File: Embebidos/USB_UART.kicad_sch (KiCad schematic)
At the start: 9 parts

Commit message: Corrección de anotaciones
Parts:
- renumbered C2 to C5, C3 to C6, C1 to C7, Q2 to Q1, Q1 to Q2, R1 to R12, R2 to R13
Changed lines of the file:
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@@
   (symbol (lib_id "power:VBUS") (at 102.87 86.36 0) (unit 1)
     (in_bom yes) (on_board yes) (fields_autoplaced)
-    (property "Reference" "#PWR?" (id 0) (at 102.87 90.17 0)
+    (property "Reference" "#PWR013" (id 0) (at 102.87 90.17 0)
       (effects (font (size 1.27 1.27)) hide)
     )
@@
   (symbol (lib_id "power:GND") (at 130.81 130.81 0) (unit 1)
     (in_bom yes) (on_board yes) (fields_autoplaced)
-    (property "Reference" "#PWR?" (id 0) (at 130.81 137.16 0)
+    (property "Reference" "#PWR016" (id 0) (at 130.81 137.16 0)
       (effects (font (size 1.27 1.27)) hide)
     )
@@
   (symbol (lib_id "Device:R") (at 184.15 90.17 90) (unit 1)
     (in_bom yes) (on_board yes) (fields_autoplaced)
-    (property "Reference" "R1" (id 0) (at 184.15 83.82 90))
+    (property "Reference" "R12" (id 0) (at 184.15 83.82 90))
     (property "Value" "~" (id 1) (at 184.15 86.36 90))
     (property "Footprint" "" (id 2) (at 184.15 91.948 90)
@@
   (symbol (lib_id "power:GND") (at 111.76 130.81 0) (unit 1)
     (in_bom yes) (on_board yes) (fields_autoplaced)
-    (property "Reference" "#PWR?" (id 0) (at 111.76 137.16 0)
+    (property "Reference" "#PWR014" (id 0) (at 111.76 137.16 0)
       (effects (font (size 1.27 1.27)) hide)
     )
@@
   (symbol (lib_id "power:GND") (at 92.71 129.54 0) (unit 1)
     (in_bom yes) (on_board yes) (fields_autoplaced)
-    (property "Reference" "#PWR?" (id 0) (at 92.71 135.89 0)
+    (property "Reference" "#PWR012" (id 0) (at 92.71 135.89 0)
       (effects (font (size 1.27 1.27)) hide)
     )
@@
   (symbol (lib_id "power:+3.3V") (at 92.71 116.84 0) (unit 1)
     (in_bom yes) (on_board yes) (fields_autoplaced)
-    (property "Reference" "#PWR?" (id 0) (at 92.71 120.65 0)
+    (property "Reference" "#PWR011" (id 0) (at 92.71 120.65 0)
       (effects (font (size 1.27 1.27)) hide)
     )
@@
   (symbol (lib_id "Device:C") (at 97.79 123.19 0) (unit 1)
     (in_bom yes) (on_board yes) (fields_autoplaced)
-    (property "Reference" "C3" (id 0) (at 101.6 121.9199 0)
+    (property "Reference" "C6" (id 0) (at 101.6 121.9199 0)
       (effects (font (size 1.27 1.27)) (justify left))
     )
@@
   (symbol (lib_id "Transistor_BJT:BC847") (at 196.85 114.3 0) (mirror x) (unit 1)
     (in_bom yes) (on_board yes) (fields_autoplaced)
-    (property "Reference" "Q1" (id 0) (at 201.93 113.0299 0)
+    (property "Reference" "Q2" (id 0) (at 201.93 113.0299 0)
       (effects (font (size 1.27 1.27)) (justify left))
     )
@@
   (symbol (lib_id "power:GND") (at 81.28 104.14 0) (unit 1)
     (in_bom yes) (on_board yes) (fields_autoplaced)
-    (property "Reference" "#PWR?" (id 0) (at 81.28 110.49 0)
+    (property "Reference" "#PWR010" (id 0) (at 81.28 110.49 0)
       (effects (font (size 1.27 1.27)) hide)
     )
@@
   (symbol (lib_id "power:+3.3V") (at 130.81 66.04 0) (unit 1)
     (in_bom yes) (on_board yes) (fields_autoplaced)
-    (property "Reference" "#PWR?" (id 0) (at 130.81 69.85 0)
+    (property "Reference" "#PWR015" (id 0) (at 130.81 69.85 0)
       (effects (font (size 1.27 1.27)) hide)
     )
@@
   (symbol (lib_id "Device:C") (at 86.36 123.19 0) (unit 1)
     (in_bom yes) (on_board yes) (fields_autoplaced)
-    (property "Reference" "C2" (id 0) (at 90.17 121.9199 0)
+    (property "Reference" "C5" (id 0) (at 90.17 121.9199 0)
       (effects (font (size 1.27 1.27)) (justify left))
     )
@@
   (symbol (lib_id "Device:R") (at 184.15 114.3 90) (unit 1)
     (in_bom yes) (on_board yes) (fields_autoplaced)
-    (property "Reference" "R2" (id 0) (at 184.15 107.95 90))
+    (property "Reference" "R13" (id 0) (at 184.15 107.95 90))
     (property "Value" "~" (id 1) (at 184.15 110.49 90))
     (property "Footprint" "" (id 2) (at 184.15 116.078 90)
@@
   (symbol (lib_id "Device:C") (at 111.76 124.46 0) (unit 1)
     (in_bom yes) (on_board yes) (fields_autoplaced)
-    (property "Reference" "C1" (id 0) (at 115.57 123.1899 0)
+    (property "Reference" "C7" (id 0) (at 115.57 123.1899 0)
       (effects (font (size 1.27 1.27)) (justify left))
     )
@@
   (symbol (lib_id "Transistor_BJT:BC847") (at 196.85 90.17 0) (unit 1)
     (in_bom yes) (on_board yes) (fields_autoplaced)
-    (property "Reference" "Q2" (id 0) (at 201.93 88.8999 0)
-      (effects (font (size 1.27 1.27)) (justify left))
-    )
+    (property "Reference" "Q1" (id 0) (at 201.93 88.8999 0)
+      (effects (font (size 1.27 1.27)) (justify left))
+    )

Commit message: anotaciones_fix
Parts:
- renumbered R12 to R13, R13 to R14
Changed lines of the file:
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@@
   (symbol (lib_id "power:VBUS") (at 102.87 86.36 0) (unit 1)
     (in_bom yes) (on_board yes) (fields_autoplaced)
-    (property "Reference" "#PWR013" (id 0) (at 102.87 90.17 0)
+    (property "Reference" "#PWR014" (id 0) (at 102.87 90.17 0)
       (effects (font (size 1.27 1.27)) hide)
     )
@@
   (symbol (lib_id "power:GND") (at 130.81 130.81 0) (unit 1)
     (in_bom yes) (on_board yes) (fields_autoplaced)
-    (property "Reference" "#PWR016" (id 0) (at 130.81 137.16 0)
+    (property "Reference" "#PWR017" (id 0) (at 130.81 137.16 0)
       (effects (font (size 1.27 1.27)) hide)
     )
@@
   (symbol (lib_id "Device:R") (at 184.15 90.17 90) (unit 1)
     (in_bom yes) (on_board yes) (fields_autoplaced)
-    (property "Reference" "R12" (id 0) (at 184.15 83.82 90))
+    (property "Reference" "R13" (id 0) (at 184.15 83.82 90))
     (property "Value" "~" (id 1) (at 184.15 86.36 90))
     (property "Footprint" "" (id 2) (at 184.15 91.948 90)
@@
   (symbol (lib_id "power:GND") (at 111.76 130.81 0) (unit 1)
     (in_bom yes) (on_board yes) (fields_autoplaced)
-    (property "Reference" "#PWR014" (id 0) (at 111.76 137.16 0)
+    (property "Reference" "#PWR015" (id 0) (at 111.76 137.16 0)
       (effects (font (size 1.27 1.27)) hide)
     )
@@
   (symbol (lib_id "power:GND") (at 92.71 129.54 0) (unit 1)
     (in_bom yes) (on_board yes) (fields_autoplaced)
-    (property "Reference" "#PWR012" (id 0) (at 92.71 135.89 0)
+    (property "Reference" "#PWR013" (id 0) (at 92.71 135.89 0)
       (effects (font (size 1.27 1.27)) hide)
     )
@@
   (symbol (lib_id "power:+3.3V") (at 92.71 116.84 0) (unit 1)
     (in_bom yes) (on_board yes) (fields_autoplaced)
-    (property "Reference" "#PWR011" (id 0) (at 92.71 120.65 0)
+    (property "Reference" "#PWR012" (id 0) (at 92.71 120.65 0)
       (effects (font (size 1.27 1.27)) hide)
     )
@@
   (symbol (lib_id "power:GND") (at 81.28 104.14 0) (unit 1)
     (in_bom yes) (on_board yes) (fields_autoplaced)
-    (property "Reference" "#PWR010" (id 0) (at 81.28 110.49 0)
+    (property "Reference" "#PWR011" (id 0) (at 81.28 110.49 0)
       (effects (font (size 1.27 1.27)) hide)
     )
@@
   (symbol (lib_id "power:+3.3V") (at 130.81 66.04 0) (unit 1)
     (in_bom yes) (on_board yes) (fields_autoplaced)
-    (property "Reference" "#PWR015" (id 0) (at 130.81 69.85 0)
+    (property "Reference" "#PWR016" (id 0) (at 130.81 69.85 0)
       (effects (font (size 1.27 1.27)) hide)
     )
@@
   (symbol (lib_id "Device:R") (at 184.15 114.3 90) (unit 1)
     (in_bom yes) (on_board yes) (fields_autoplaced)
-    (property "Reference" "R13" (id 0) (at 184.15 107.95 90))
+    (property "Reference" "R14" (id 0) (at 184.15 107.95 90))
     (property "Value" "~" (id 1) (at 184.15 110.49 90))
     (property "Footprint" "" (id 2) (at 184.15 116.078 90)

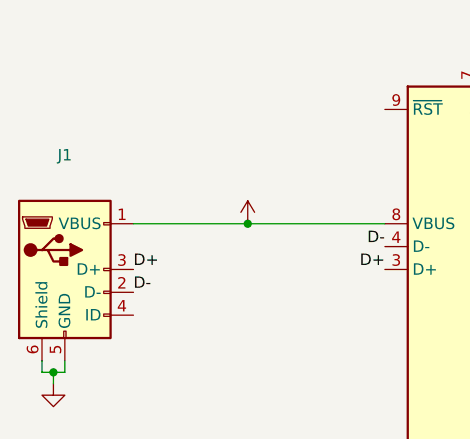
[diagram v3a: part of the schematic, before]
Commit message: Cambio de anotacion y Vcc ldr
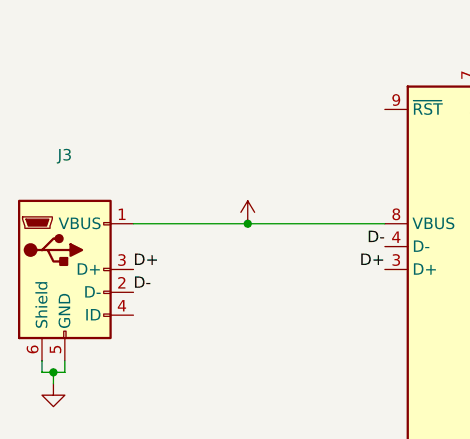
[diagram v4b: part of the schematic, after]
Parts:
- renumbered J1 to J3
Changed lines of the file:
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@@
   (symbol (lib_id "Connector:USB_B_Micro") (at 82.55 91.44 0) (unit 1)
     (in_bom yes) (on_board yes) (fields_autoplaced)
-    (property "Reference" "J1" (id 0) (at 82.55 78.74 0))
+    (property "Reference" "J3" (id 0) (at 82.55 78.74 0))
     (property "Value" "~" (id 1) (at 82.55 81.28 0))
     (property "Footprint" "" (id 2) (at 86.36 92.71 0)
@@
   (symbol (lib_id "power:VBUS") (at 102.87 86.36 0) (unit 1)
     (in_bom yes) (on_board yes) (fields_autoplaced)
-    (property "Reference" "#PWR014" (id 0) (at 102.87 90.17 0)
+    (property "Reference" "#PWR017" (id 0) (at 102.87 90.17 0)
       (effects (font (size 1.27 1.27)) hide)
     )
@@
   (symbol (lib_id "power:GND") (at 130.81 130.81 0) (unit 1)
     (in_bom yes) (on_board yes) (fields_autoplaced)
-    (property "Reference" "#PWR017" (id 0) (at 130.81 137.16 0)
+    (property "Reference" "#PWR020" (id 0) (at 130.81 137.16 0)
       (effects (font (size 1.27 1.27)) hide)
     )
@@
   (symbol (lib_id "power:GND") (at 111.76 130.81 0) (unit 1)
     (in_bom yes) (on_board yes) (fields_autoplaced)
-    (property "Reference" "#PWR015" (id 0) (at 111.76 137.16 0)
+    (property "Reference" "#PWR018" (id 0) (at 111.76 137.16 0)
       (effects (font (size 1.27 1.27)) hide)
     )
@@
   (symbol (lib_id "power:GND") (at 92.71 129.54 0) (unit 1)
     (in_bom yes) (on_board yes) (fields_autoplaced)
-    (property "Reference" "#PWR013" (id 0) (at 92.71 135.89 0)
+    (property "Reference" "#PWR016" (id 0) (at 92.71 135.89 0)
       (effects (font (size 1.27 1.27)) hide)
     )
@@
   (symbol (lib_id "power:+3.3V") (at 92.71 116.84 0) (unit 1)
     (in_bom yes) (on_board yes) (fields_autoplaced)
-    (property "Reference" "#PWR012" (id 0) (at 92.71 120.65 0)
+    (property "Reference" "#PWR015" (id 0) (at 92.71 120.65 0)
       (effects (font (size 1.27 1.27)) hide)
     )
@@
   (symbol (lib_id "power:GND") (at 81.28 104.14 0) (unit 1)
     (in_bom yes) (on_board yes) (fields_autoplaced)
-    (property "Reference" "#PWR011" (id 0) (at 81.28 110.49 0)
+    (property "Reference" "#PWR014" (id 0) (at 81.28 110.49 0)
       (effects (font (size 1.27 1.27)) hide)
     )
@@
   (symbol (lib_id "power:+3.3V") (at 130.81 66.04 0) (unit 1)
     (in_bom yes) (on_board yes) (fields_autoplaced)
-    (property "Reference" "#PWR016" (id 0) (at 130.81 69.85 0)
+    (property "Reference" "#PWR019" (id 0) (at 130.81 69.85 0)
       (effects (font (size 1.27 1.27)) hide)
     )

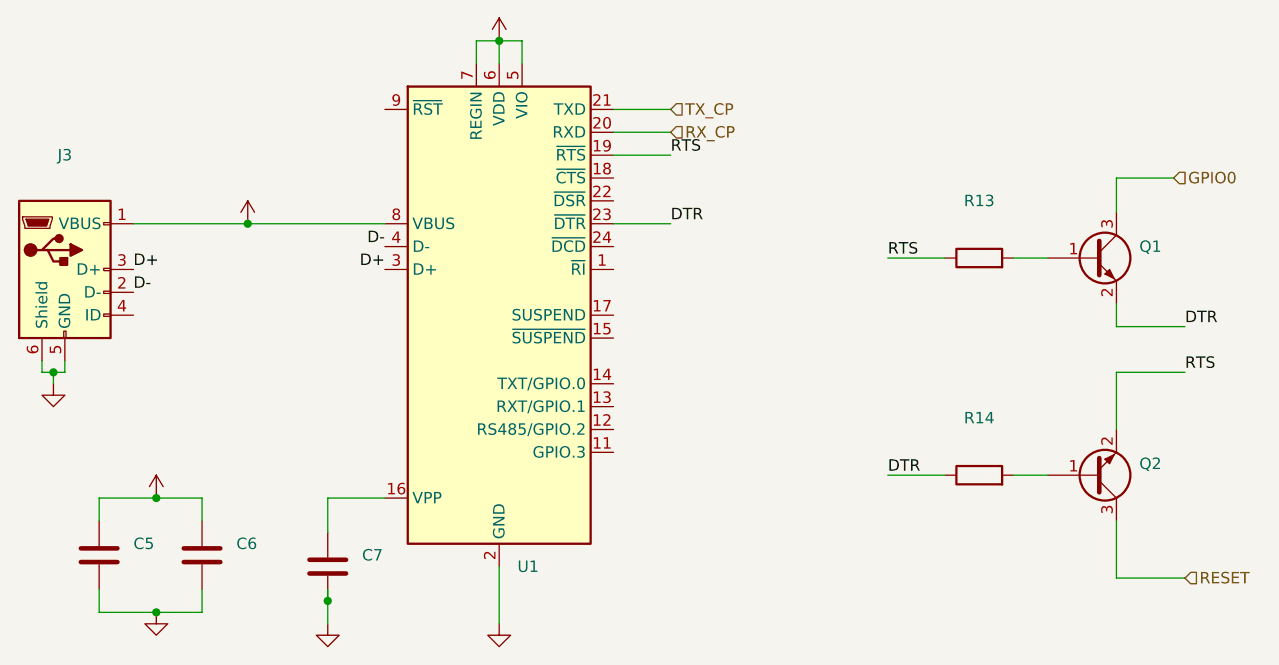
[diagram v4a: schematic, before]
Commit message: Cambios varios
-Conectores movidos a nueva hoja jerarquica

-Transistores DMP colocados en lices delanteras

-Jumpers ubicados para el uso del pin IO13 para SIM800 y LEDHW

-Etiqueta de "no conectado" ubicada en USB_UART
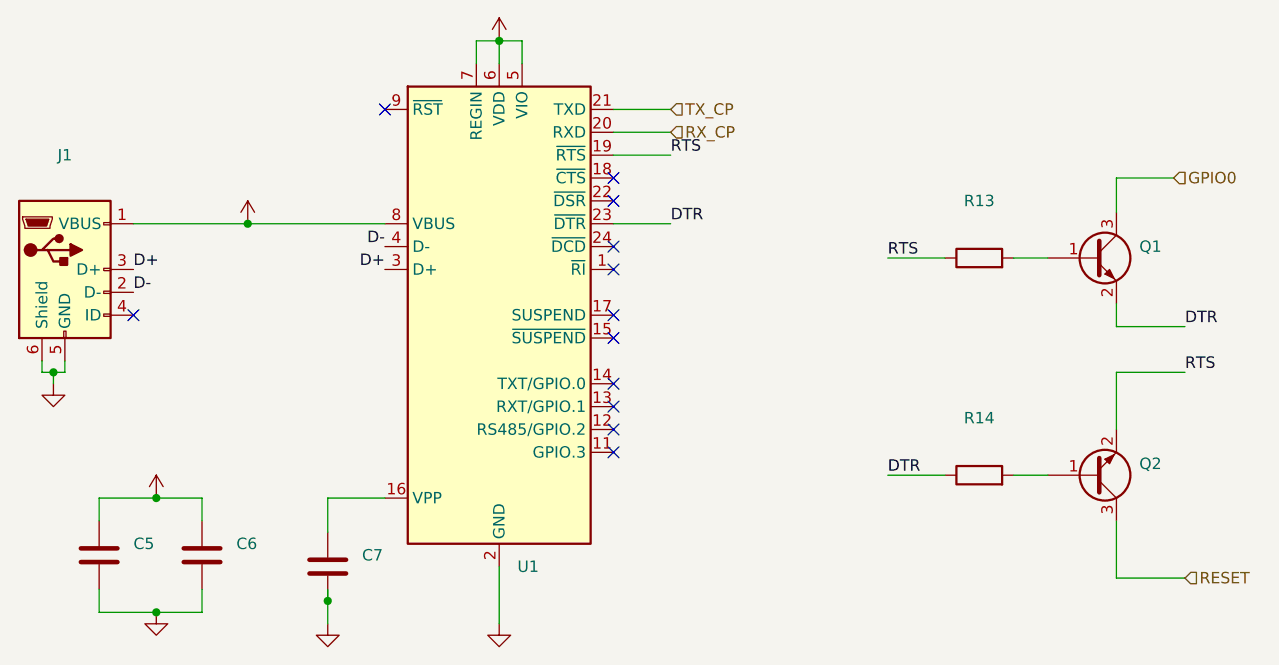
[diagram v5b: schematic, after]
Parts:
- renumbered J3 to J1
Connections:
- no-connect marks 0 -> 12
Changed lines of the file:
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@@
   (junction (at 92.71 129.54) (diameter 0) (color 0 0 0 0)
   )
+  (junction (at 81.28 102.87) (diameter 0) (color 0 0 0 0)
+  )
   (junction (at 111.76 128.27) (diameter 0) (color 0 0 0 0)
   )
-  (junction (at 81.28 102.87) (diameter 0) (color 0 0 0 0)
-  )
+  (no_connect (at 90.17 96.52))
+  (no_connect (at 143.51 106.68))
+  (no_connect (at 143.51 109.22))
+  (no_connect (at 143.51 111.76))
+  (no_connect (at 118.11 73.66))
+  (no_connect (at 143.51 81.28))
+  (no_connect (at 143.51 83.82))
+  (no_connect (at 143.51 88.9))
+  (no_connect (at 143.51 91.44))
+  (no_connect (at 143.51 96.52))
+  (no_connect (at 143.51 99.06))
+  (no_connect (at 143.51 104.14))
   (wire (pts (xy 102.87 86.36) (xy 118.11 86.36))
     (stroke (width 0) (type default) (color 0 0 0 0))
@@
     (stroke (width 0) (type default) (color 0 0 0 0))
   )
+  (wire (pts (xy 80.01 101.6) (xy 80.01 102.87))
+    (stroke (width 0) (type default) (color 0 0 0 0))
+  )
   (wire (pts (xy 128.27 68.58) (xy 128.27 66.04))
     (stroke (width 0) (type default) (color 0 0 0 0))
@@
     (stroke (width 0) (type default) (color 0 0 0 0))
   )
+  (wire (pts (xy 80.01 102.87) (xy 81.28 102.87))
+    (stroke (width 0) (type default) (color 0 0 0 0))
+  )
+  (wire (pts (xy 81.28 102.87) (xy 81.28 104.14))
+    (stroke (width 0) (type default) (color 0 0 0 0))
+  )
   (wire (pts (xy 130.81 124.46) (xy 130.81 130.81))
     (stroke (width 0) (type default) (color 0 0 0 0))
   )
-  (wire (pts (xy 80.01 102.87) (xy 81.28 102.87))
-    (stroke (width 0) (type default) (color 0 0 0 0))
-  )
   (wire (pts (xy 143.51 78.74) (xy 149.86 78.74))
     (stroke (width 0) (type default) (color 0 0 0 0))
@@
     (stroke (width 0) (type default) (color 0 0 0 0))
   )
+  (wire (pts (xy 199.39 95.25) (xy 199.39 97.79))
+    (stroke (width 0) (type default) (color 0 0 0 0))
+  )
+  (wire (pts (xy 207.01 102.87) (xy 199.39 102.87))
+    (stroke (width 0) (type default) (color 0 0 0 0))
+  )
   (wire (pts (xy 81.28 102.87) (xy 82.55 102.87))
-    (stroke (width 0) (type default) (color 0 0 0 0))
-  )
-  (wire (pts (xy 81.28 102.87) (xy 81.28 104.14))
-    (stroke (width 0) (type default) (color 0 0 0 0))
-  )
-  (wire (pts (xy 199.39 95.25) (xy 199.39 97.79))
-    (stroke (width 0) (type default) (color 0 0 0 0))
-  )
-  (wire (pts (xy 80.01 101.6) (xy 80.01 102.87))
-    (stroke (width 0) (type default) (color 0 0 0 0))
-  )
-  (wire (pts (xy 207.01 102.87) (xy 199.39 102.87))
     (stroke (width 0) (type default) (color 0 0 0 0))
   )
@@
   (symbol (lib_id "Connector:USB_B_Micro") (at 82.55 91.44 0) (unit 1)
     (in_bom yes) (on_board yes) (fields_autoplaced)
-    (property "Reference" "J3" (id 0) (at 82.55 78.74 0))
+    (property "Reference" "J1" (id 0) (at 82.55 78.74 0))
     (property "Value" "~" (id 1) (at 82.55 81.28 0))
     (property "Footprint" "" (id 2) (at 86.36 92.71 0)
@@
   (symbol (lib_id "power:VBUS") (at 102.87 86.36 0) (unit 1)
     (in_bom yes) (on_board yes) (fields_autoplaced)
-    (property "Reference" "#PWR017" (id 0) (at 102.87 90.17 0)
+    (property "Reference" "#PWR014" (id 0) (at 102.87 90.17 0)
       (effects (font (size 1.27 1.27)) hide)
     )
@@
   (symbol (lib_id "power:GND") (at 130.81 130.81 0) (unit 1)
     (in_bom yes) (on_board yes) (fields_autoplaced)
-    (property "Reference" "#PWR020" (id 0) (at 130.81 137.16 0)
+    (property "Reference" "#PWR017" (id 0) (at 130.81 137.16 0)
       (effects (font (size 1.27 1.27)) hide)
     )
@@
   (symbol (lib_id "power:GND") (at 111.76 130.81 0) (unit 1)
     (in_bom yes) (on_board yes) (fields_autoplaced)
-    (property "Reference" "#PWR018" (id 0) (at 111.76 137.16 0)
+    (property "Reference" "#PWR015" (id 0) (at 111.76 137.16 0)
       (effects (font (size 1.27 1.27)) hide)
     )
@@
   (symbol (lib_id "power:GND") (at 92.71 129.54 0) (unit 1)
     (in_bom yes) (on_board yes) (fields_autoplaced)
-    (property "Reference" "#PWR016" (id 0) (at 92.71 135.89 0)
+    (property "Reference" "#PWR013" (id 0) (at 92.71 135.89 0)
       (effects (font (size 1.27 1.27)) hide)
     )
@@
   (symbol (lib_id "power:+3.3V") (at 92.71 116.84 0) (unit 1)
     (in_bom yes) (on_board yes) (fields_autoplaced)
-    (property "Reference" "#PWR015" (id 0) (at 92.71 120.65 0)
+    (property "Reference" "#PWR012" (id 0) (at 92.71 120.65 0)
       (effects (font (size 1.27 1.27)) hide)
     )
@@
   (symbol (lib_id "power:GND") (at 81.28 104.14 0) (unit 1)
     (in_bom yes) (on_board yes) (fields_autoplaced)
-    (property "Reference" "#PWR014" (id 0) (at 81.28 110.49 0)
+    (property "Reference" "#PWR011" (id 0) (at 81.28 110.49 0)
       (effects (font (size 1.27 1.27)) hide)
     )
@@
   (symbol (lib_id "power:+3.3V") (at 130.81 66.04 0) (unit 1)
     (in_bom yes) (on_board yes) (fields_autoplaced)
-    (property "Reference" "#PWR019" (id 0) (at 130.81 69.85 0)
-      (effects (font (size 1.27 1.27)) hide)
-    )
+    (property "Reference" "#PWR016" (id 0) (at 130.81 69.85 0)
+      (effects (font (size 1.27 1.27)) hide)
+    )
